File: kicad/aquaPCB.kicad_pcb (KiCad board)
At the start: 2 copper layers, 100 x 100 mm, 149 parts, among them J1 12V IN, J11 SSR G17, J12 SSR G22, J13 SSR G23, J14 SSR G27, J15 IN1, J16 IN2, J17 IN3, J18 IN4, J19 1-Wire 1, J2 Raspberry Pi, J22 I2C 1, J23 I2C 2, J24 Display, J25 pH probe, J26 Module, J27 AIN3, J4 OUT G18, J5 OUT G19, J6 OUT G12, J7 OUT G13, J8 OUT G16, J9 OUT G26, Q1 AOD4184A, Q10 AOD4185, Q2 AOD4184A, Q3 AOD4184A, Q4 AOD4184A, Q5 AOD4184A, Q6 AOD4184A, U1 TPS54360B, U2 AMS1117-3.3, U3 74HCT244D, U4 ULN2803A, U5 ADS1115IDGSR, U6 TLV9062IDR

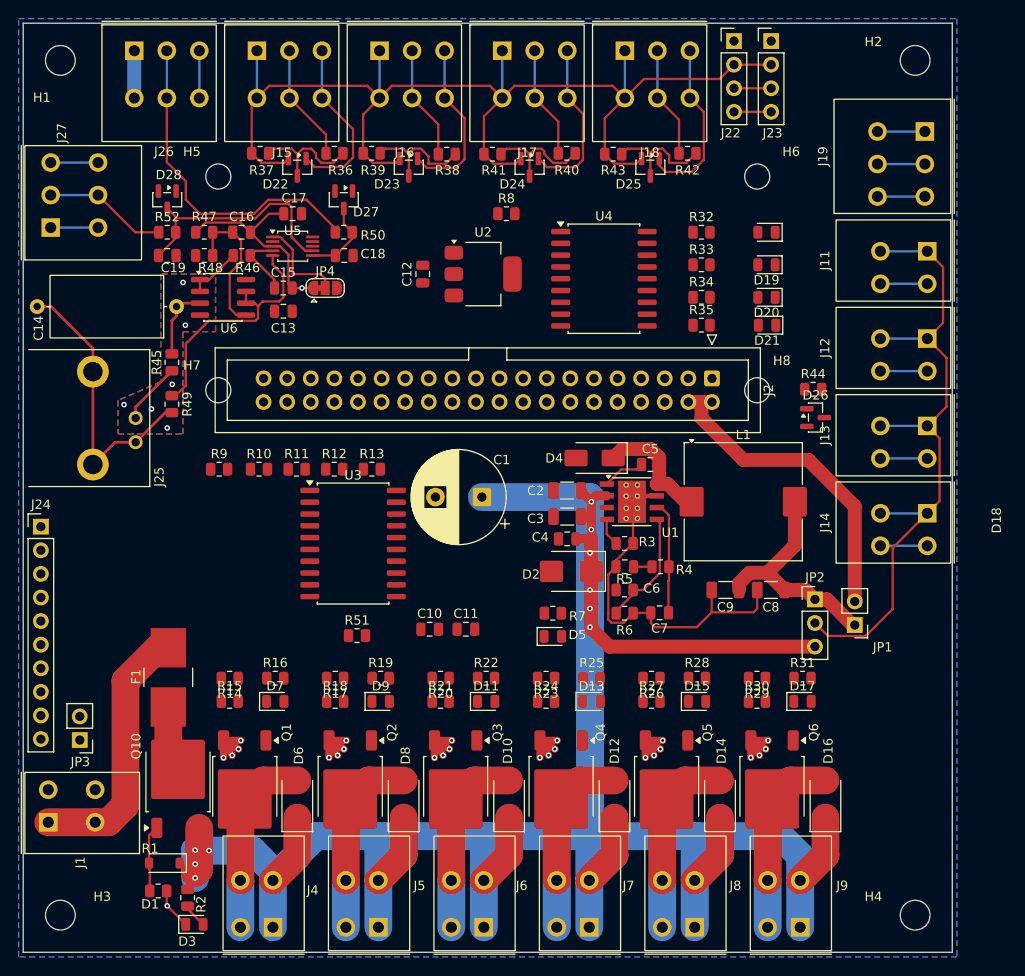
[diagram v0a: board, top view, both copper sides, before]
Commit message: kicad: routing progress (by hand)
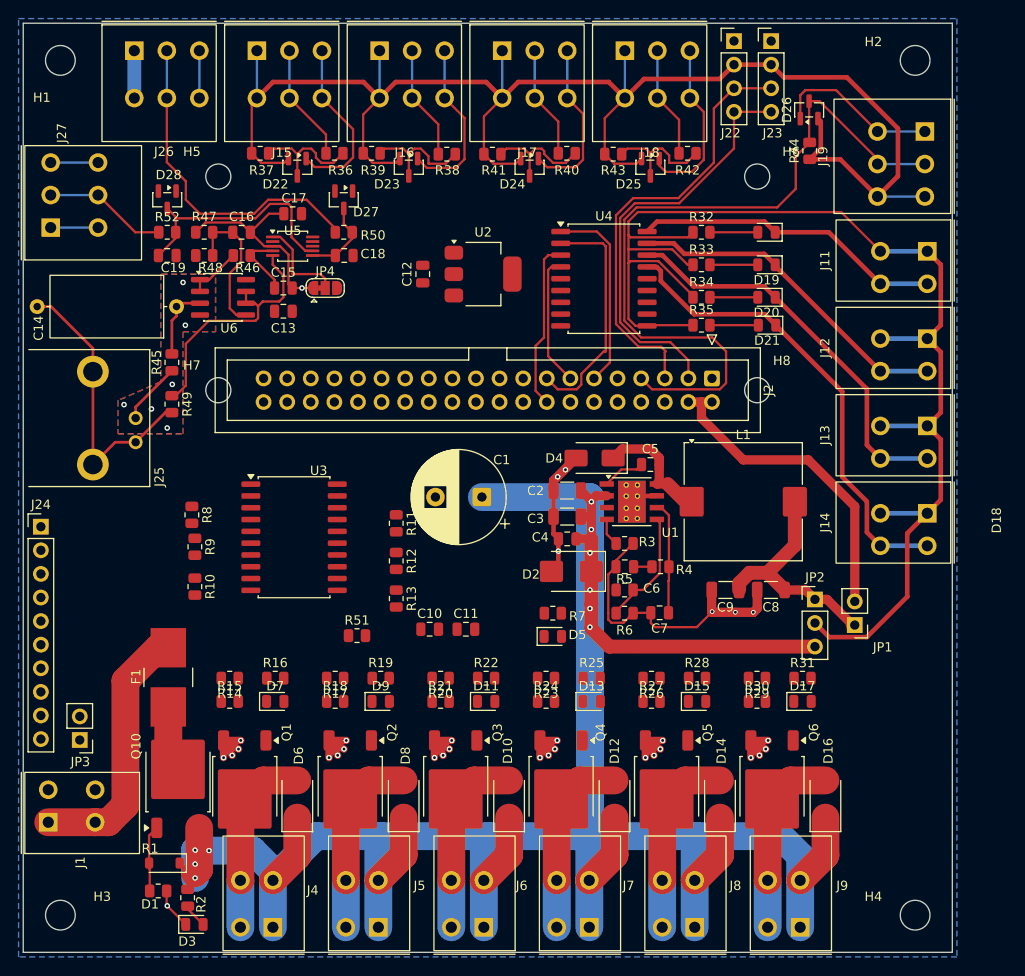
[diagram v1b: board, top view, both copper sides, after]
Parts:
- moved R8 46.9 mm to (97.0, 88.6), turned to -90 degrees
- moved D26 33.1 mm to (163.4, 45.0), turned to 90 degrees
- moved R44 25.7 mm to (163.5, 49.4), turned to 90 degrees
- moved R10 14.4 mm to (97.3, 96.3), turned to -90 degrees
- moved R13 14.2 mm to (119.0, 97.6), turned to -90 degrees
- moved R11 12.2 mm to (119.0, 89.5), turned to -90 degrees
- moved R12 11.9 mm to (119.0, 93.5), turned to -90 degrees
- moved R9 8.75 mm to (97.3, 92.0), turned to -90 degrees
- moved U3 6.39 mm to (108.0, 91.0)
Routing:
- net GPIO4_1W: track 5.10 -> 82.0 mm
- net /SSR / relay control outputs S1..S4/SSR_V: track 74.6 -> 144.9 mm
- net /SSR / relay control outputs S1..S4/S4_OUT: track 5.05 -> 50.5 mm
- net GPIO3_SCL: track 4.00 -> 47.0 mm
- net GPIO2_SDA: track 4.00 -> 45.5 mm
- net +3V3: track 136.2 -> 175.9 mm
- net /SSR / relay control outputs S1..S4/S3_OUT: track 5.05 -> 42.8 mm
- net /SSR / relay control outputs S1..S4/S2_OUT: track 5.05 -> 35.9 mm
- net /SSR / relay control outputs S1..S4/S1_OUT: track 5.05 -> 33.4 mm
- net GPIO22_S2: track 0.00 -> 25.5 mm
- net GND: track 197.8 -> 221.5 mm, vias 26 -> 32
- net GPIO17_S1: track 0.00 -> 21.0 mm
- net GPIO23_S3: track 0.00 -> 18.4 mm
- net GPIO27_S4: track 0.00 -> 14.1 mm
- net /SSR / relay control outputs S1..S4/S4_LED: track 0.00 -> 5.21 mm
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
